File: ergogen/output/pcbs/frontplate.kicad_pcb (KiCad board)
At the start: 2 copper layers, 130 x 88.1 mm, 5 parts

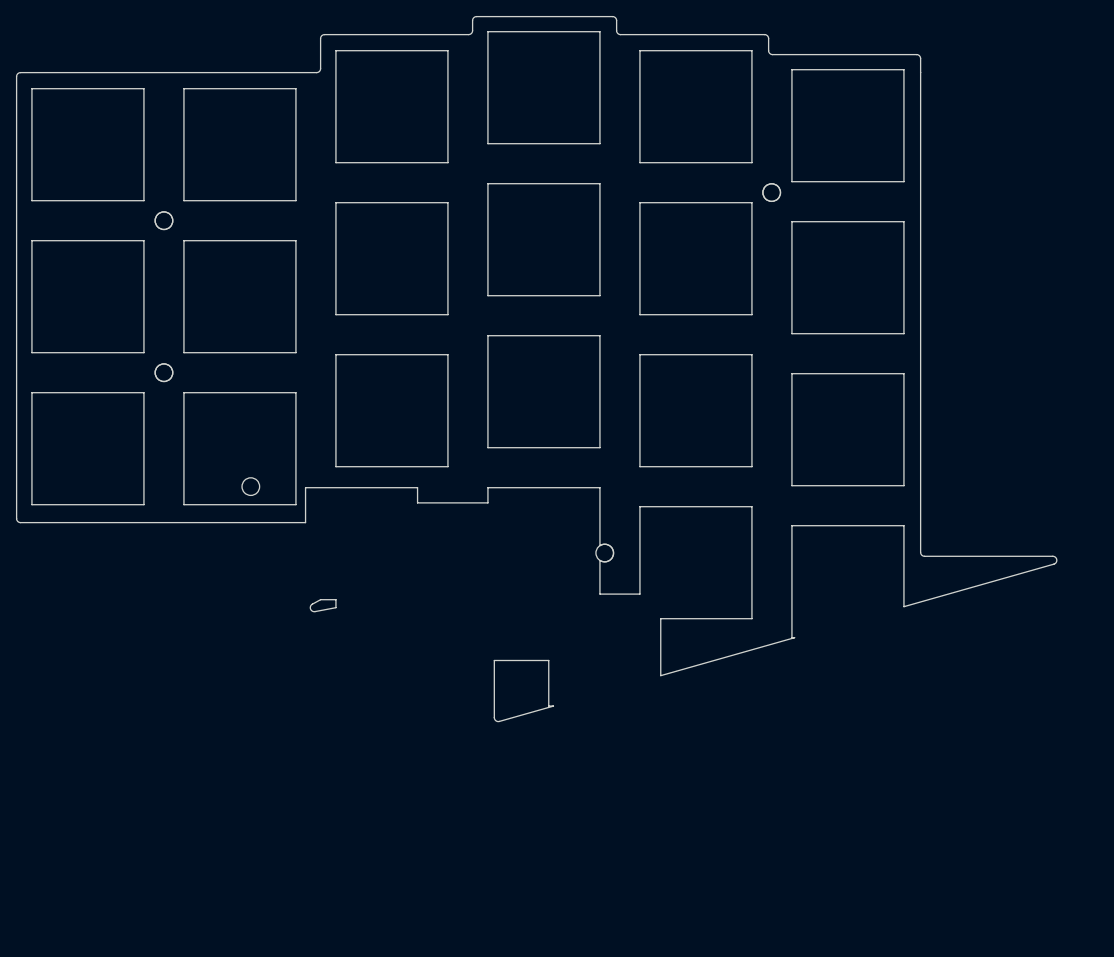
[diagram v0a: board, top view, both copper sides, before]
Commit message: feat: souffle outputs
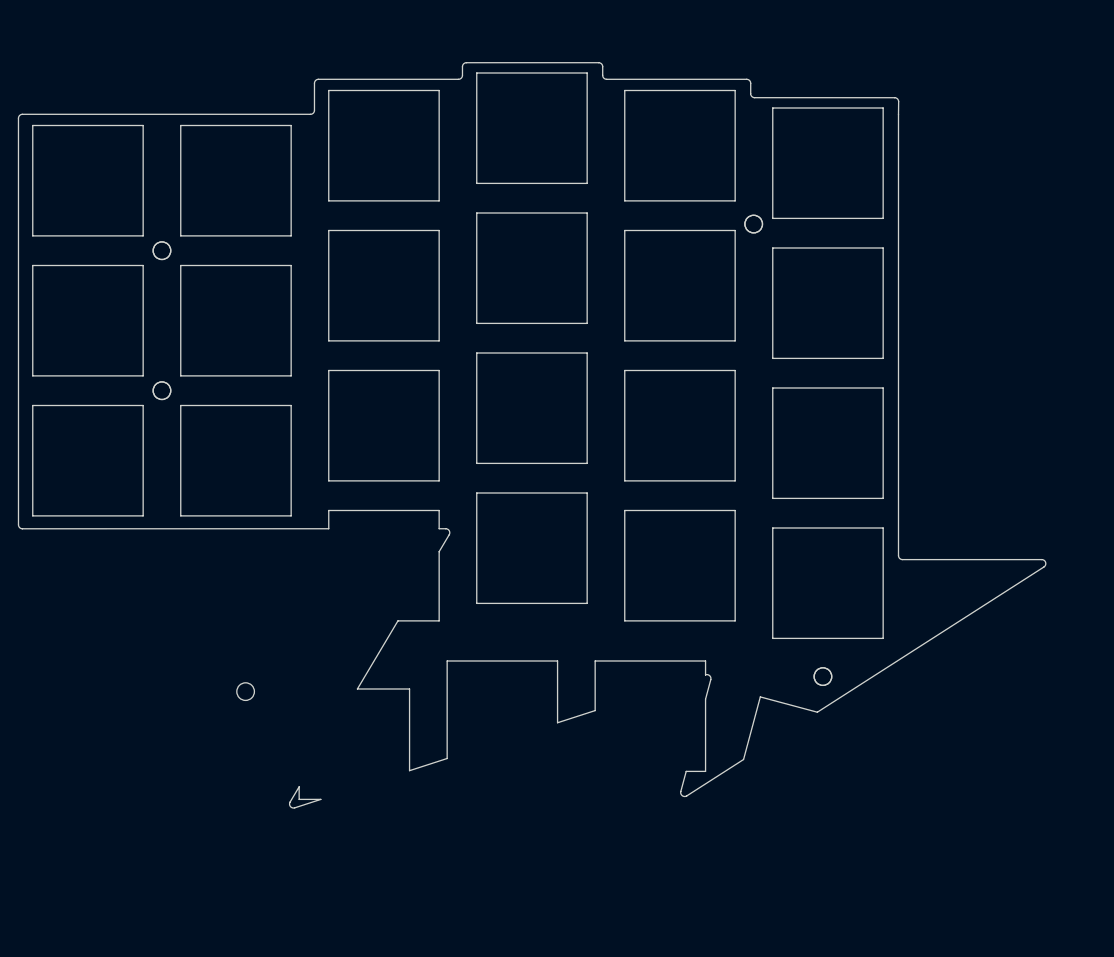
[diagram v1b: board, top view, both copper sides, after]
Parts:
- moved MH5 31.3 mm to (191.9, 109.5), turned to -15 degrees
- moved MH4 25.6 mm to (119.7, 111.4)
- moved MH3 4.54 mm to (183.2, 52.9)
- moved MH1 3.76 mm to (109.2, 56.2)
- moved MH2 2.26 mm to (109.2, 73.8)
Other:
- board size 130 x 88.1 mm -> 128.4 x 93.2 mm

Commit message: fix: number row on top and improved outline
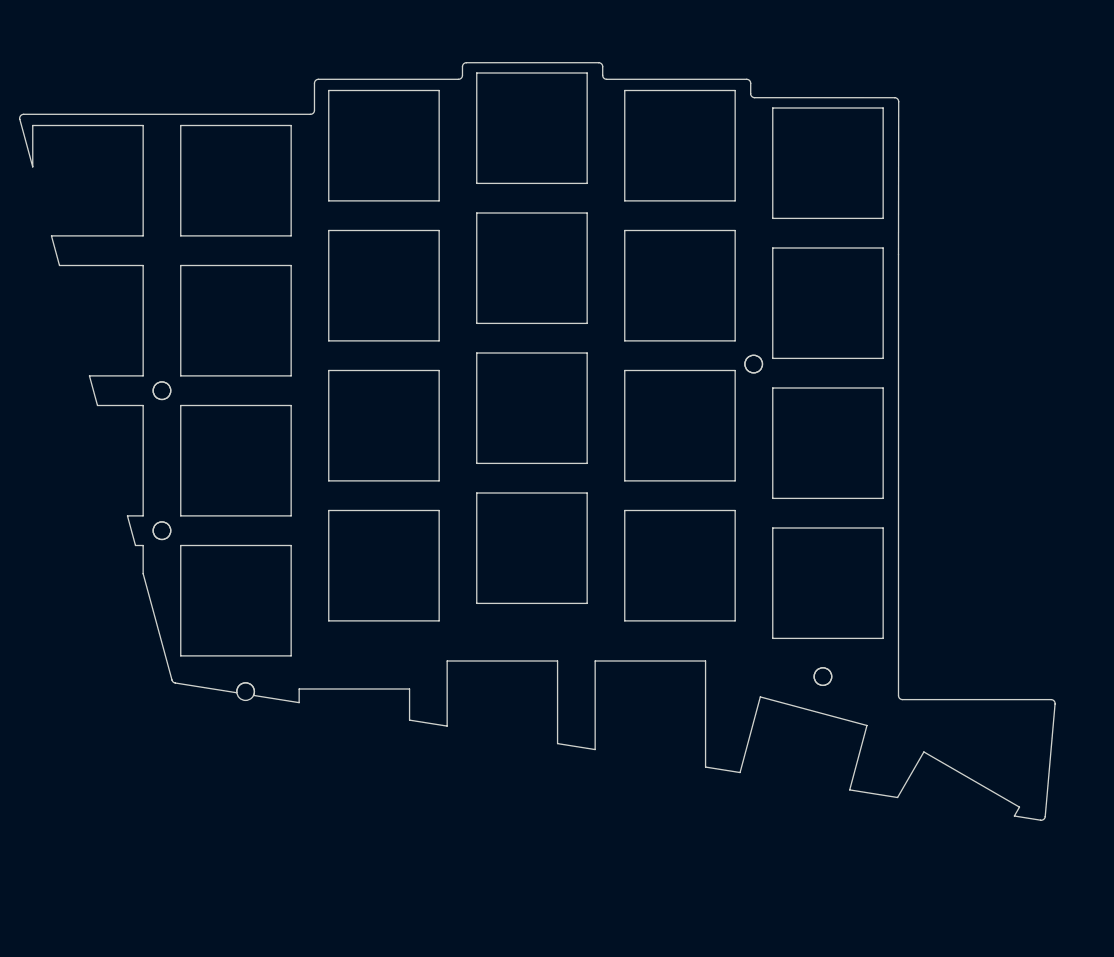
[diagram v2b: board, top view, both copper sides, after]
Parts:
- moved MH3 17.5 mm to (183.2, 70.4)
- moved MH1 17.5 mm to (109.2, 73.8)
- moved MH2 17.5 mm to (109.2, 91.2)
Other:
- board size 128.4 x 93.2 mm -> 129.4 x 94.7 mm

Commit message: feat: outline improvements
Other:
- board size 129.4 x 94.7 mm -> 134.9 x 109.8 mm

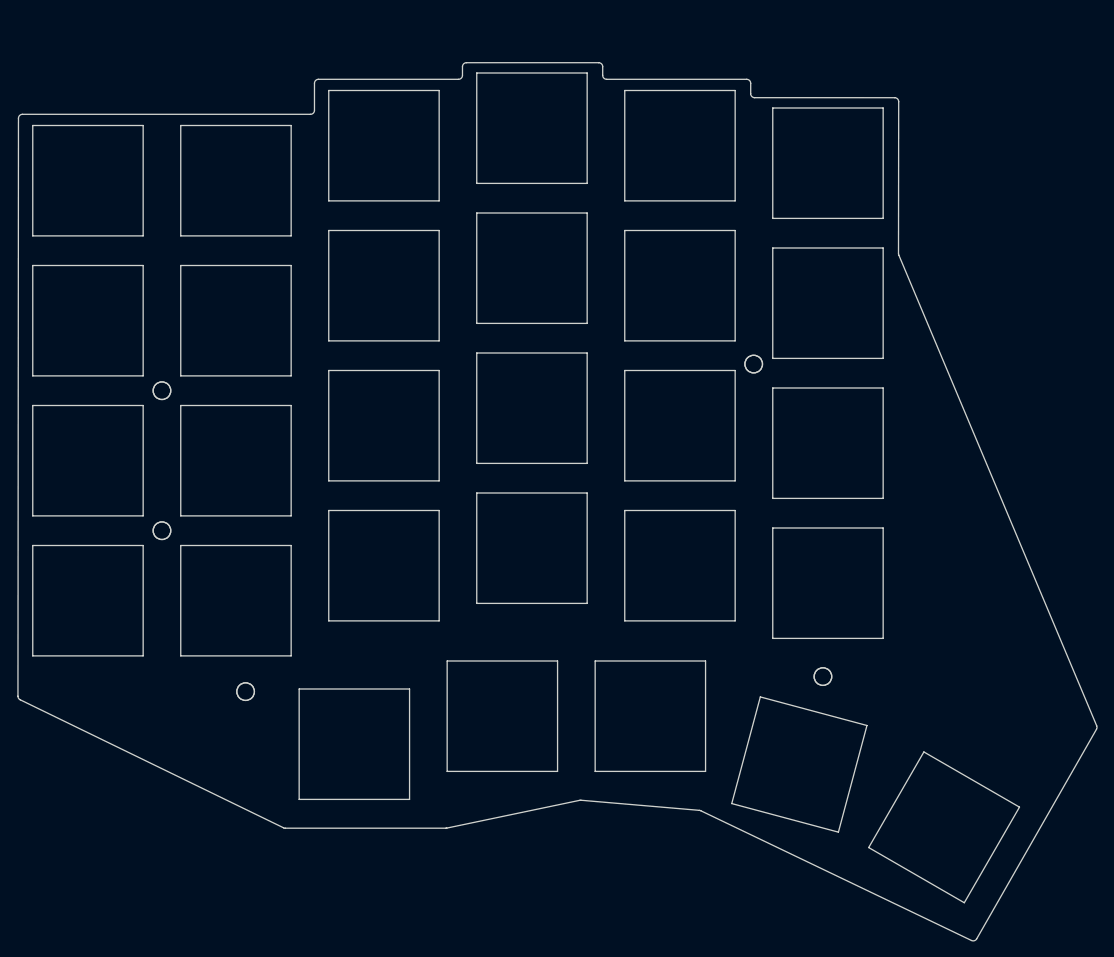
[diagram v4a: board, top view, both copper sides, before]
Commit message: feat: PCB holes alignment
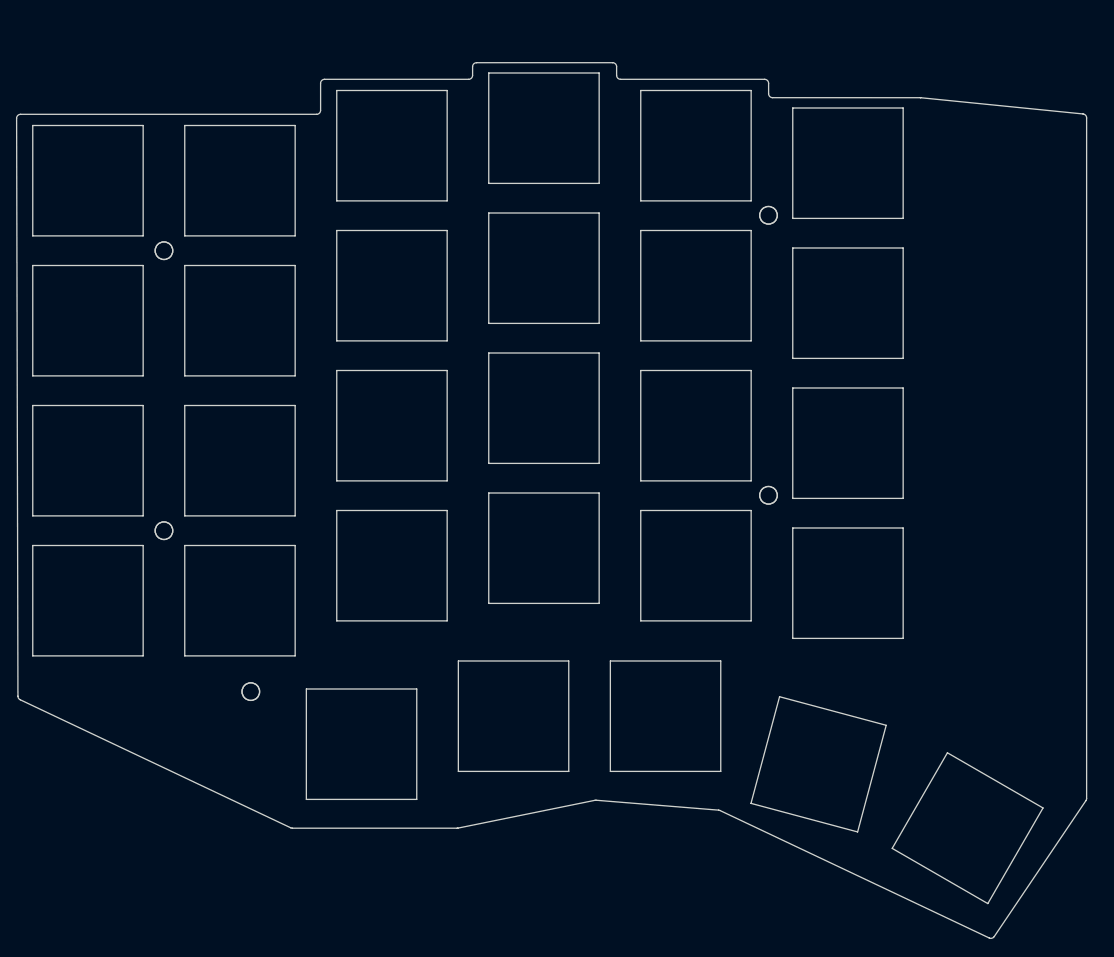
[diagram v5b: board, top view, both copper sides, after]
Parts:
- moved MH5 71.5 mm to (120.4, 111.4), turned to 0 degrees
- moved MH4 69.8 mm to (185.1, 86.8)
- moved MH3 18.7 mm to (185.1, 51.8)
- moved MH1 17.5 mm to (109.5, 56.2)
- moved MH2 0.25 mm to (109.5, 91.2)
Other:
- board size 134.9 x 109.8 mm -> 133.8 x 109.5 mm
